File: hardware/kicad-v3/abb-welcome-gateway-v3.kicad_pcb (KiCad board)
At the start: 2 copper layers, 45.3 x 53.3 mm, 69 parts, among them P1 WJ500V-5.08-2P, Q1 S8050, Q2 S8050, Q3 S8050, Q4 2N7002, Q5 2N7002, Q6 2N7002, SW1 TS-1187A-B-A-B, U1 TPS5430DDAR, U2 ESP32-S3-WROOM-1-N16R8, U3 74LVC1G14

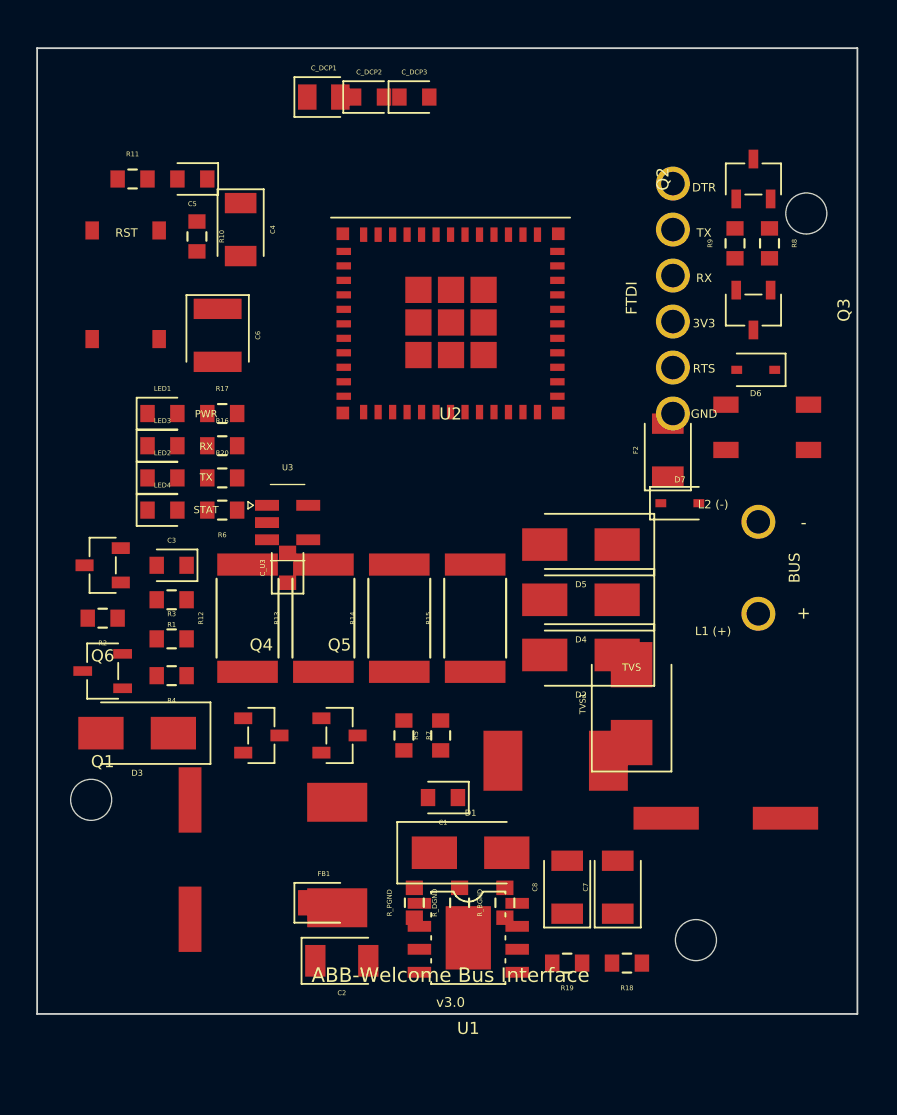
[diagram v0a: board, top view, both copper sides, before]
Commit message: PCB v3: footprint real del ESP32-S3-WROOM-1, placa a 56.4mm y placement listo para rutear
- U2: sustituido el footprint tipo QFN invalido (61 pads inventados) por
  RF_Module:ESP32-S3-WROOM-1 oficial de KiCad; nets remapeados a los pines
  reales del modulo (GND/3V3/EN/IO4/IO5/IO0/RXD0/TXD0/IO2 + EP). Antena al
  borde superior con su keep-out.
- Contorno: +3mm de alto (45.4x56.4) para dar sitio a la banda del buck.
- Placement reorganizado por islas de tierra: DGND arriba (ESP32/FTDI/reset/
  LEDs/U3), BUS_GND banda media y columna derecha (front-end RX/TX, entrada
  28V), PGND abajo (buck TPS5430 con U1 rotado 180: VIN hacia C7/C8, SW
  hacia D1/L2; feedback R18/R19 junto al pin FB; C4/C6 en su isla).
- Star point PGND/DGND/BUS_GND abajo a la derecha (R_PGND/R_BGND/R_DGND).
- Corregidas colisiones fisicas invisibles al DRC (footprints sin courtyard
  ni cuerpo: L2/L3/C19/C23/P1): FB1 bajo L2, TVS1 sobre L3, etc.
- Verificado: 0 solapes de courtyard/envolvente fisica en DRC y chequeo
  propio con cuerpos reales.
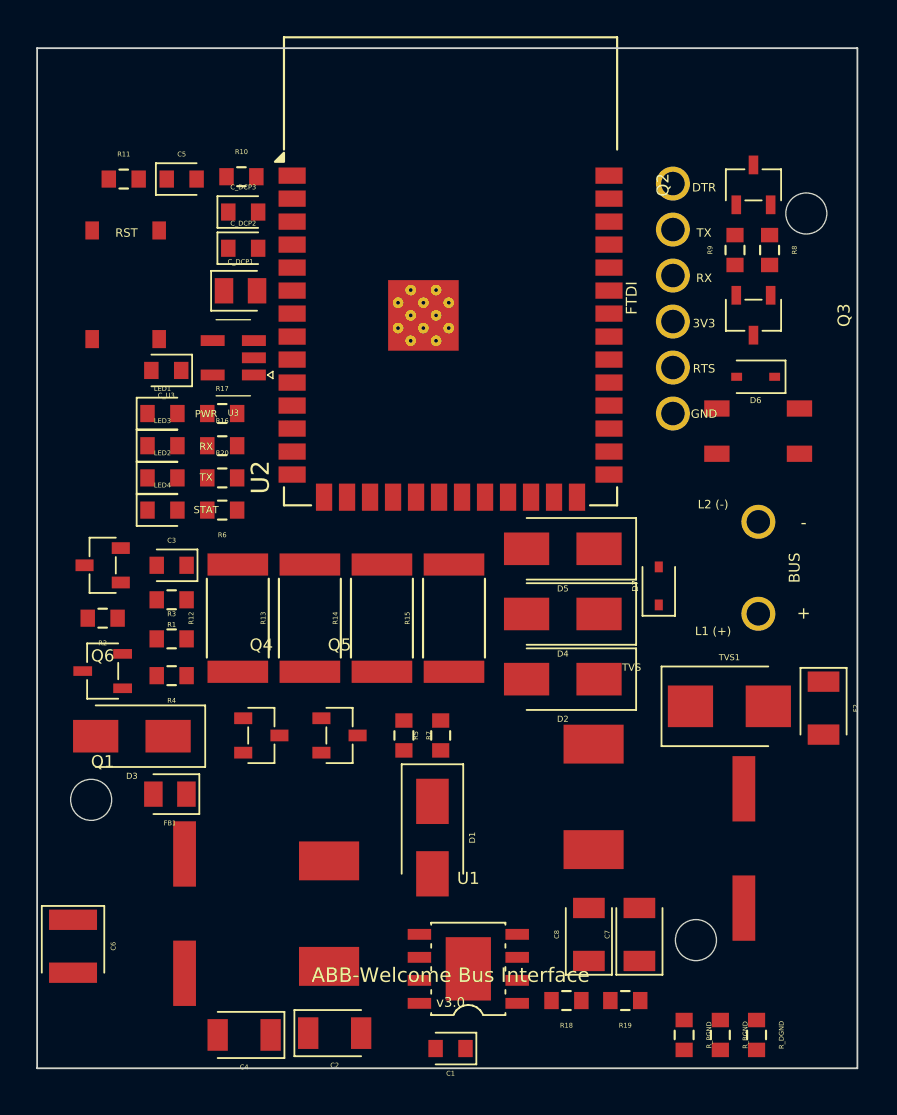
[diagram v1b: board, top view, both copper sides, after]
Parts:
- U2: footprint tscircuit:ESP32-S3-WROOM-1-N16R8 -> ESP32-S3-WROOM-1
- moved C4 44.5 mm to (88.6, 129.3), turned to 180 degrees
- moved C6 34.7 mm to (79.2, 124.4)
- moved R_DGND 18.0 mm to (116.9, 129.3), turned to -90 degrees
- moved F2 16.6 mm to (120.6, 111.2), turned to -90 degrees
- moved R_PGND 16.6 mm to (112.9, 129.3), turned to -90 degrees
- moved R_BGND 14.0 mm to (114.9, 129.3), turned to -90 degrees
- moved C1 13.9 mm to (100.0, 130.1)
- moved C_U3 12.8 mm to (84.3, 92.6), turned to 180 degrees
- moved C_DCP1 11.6 mm to (88.4, 88.2)
- moved C_DCP3 11.4 mm to (88.5, 83.8)
- moved C_DCP2 10.9 mm to (88.5, 85.8)
- moved FB1 10.4 mm to (84.5, 116.0), turned to 180 degrees
- moved U3 9.58 mm to (88.0, 91.9), turned to 180 degrees
- moved TVS1 5.40 mm to (115.4, 111.2), turned to 0 degrees
- moved D7 4.71 mm to (111.5, 104.5), turned to 90 degrees
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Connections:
- U2 pad 27: (no net) -> BOOT_STRAP
- U2 pad 36: (no net) -> RX
- U2 pad 37: (no net) -> TX
- U2 pad 38: BOOT_STRAP -> LED_PIN
- U2 pad 40: (no net) -> DGND
- U2 pad 41: (no net) -> DGND
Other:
- board size 45.3 x 53.3 mm -> 45.3 x 56.3 mm

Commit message: PCB v3: reglas de diseno, net classes y zonas de las 3 islas de GND
- .kicad_pro: minimos 0.2/0.2mm (JLCPCB 2 capas), via 0.6/0.3; clases
  Power (0.8mm), BusHV (0.8mm ancho, 0.5mm clearance para el bus 28V),
  Ground (0.5mm) con asignacion por net.
- Zonas B.Cu: plano DGND (superior + corredor por el borde este hasta el
  star point), banda BUS_GND (front-end + bolsillo de entrada de bus),
  plano PGND (banda inferior del buck). Separacion 0.3mm entre islas.
- Zonas F.Cu: refuerzo PGND (termico del buck) y BUS_GND en el bolsillo.
- El keep-out de antena del modulo mantiene sin cobre la franja superior.
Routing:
- added copper zone on B.Cu, net BUS_GND
- added copper zone on F.Cu, net BUS_GND
- added copper zone on B.Cu, net DGND
- added copper zone on B.Cu, net PGND
- added copper zone on F.Cu, net PGND
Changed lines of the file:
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@@
+		)
+	)
+	(zone
+		(net 40)
+		(net_name "BUS_GND")
+		(layer "F.Cu")
+		(name "BUSGND_top")
+		(hatch edge 0.5)
+		(connect_pads
+			(clearance 0.3)
+		)
+		(min_thickness 0.25)
+		(filled_areas_thickness no)
+		(fill yes
+			(thermal_gap 0.3)
+			(thermal_bridge_width 0.5)
+		)
+		(polygon
+			(pts
+				(xy 104.4 99.15) (xy 119.55 99.15) (xy 119.55 123.3) (xy 104.4 123.3)
+			)
+		)
+	)
+	(zone
+		(net 6)
+		(net_name "PGND")
+		(layer "F.Cu")
+		(name "PGND_top")
+		(hatch edge 0.5)
+		(connect_pads
+			(clearance 0.3)
+		)
+		(min_thickness 0.25)
+		(filled_areas_thickness no)
+		(fill yes
+			(thermal_gap 0.3)
+			(thermal_bridge_width 0.5)
+		)
+		(polygon
+			(pts
+				(xy 77.45 114.9) (xy 104.1 114.9) (xy 104.1 123.75) (xy 119.5 123.75) (xy 119.5 130.85) (xy 77.45 130.85)
+			)
+		)
+	)
+	(zone
+		(net 40)
+		(net_name "BUS_GND")
+		(layer "B.Cu")
+		(name "BUSGND_plane")
+		(hatch edge 0.5)
+		(connect_pads
+			(clearance 0.3)
+		)
+		(min_thickness 0.25)
+		(filled_areas_thickness no)
+		(fill yes
+			(thermal_gap 0.3)
+			(thermal_bridge_width 0.5)
+		)
+		(polygon
+			(pts
+				(xy 77.45 101.75) (xy 100.3 101.75) (xy 100.3 99.15) (xy 119.55 99.15) (xy 119.55 123.3) (xy 104.4 123.3)
+				(xy 104.4 114.45) (xy 77.45 114.45)
+			)
+		)
+	)
+	(zone
+		(net 1)
+		(net_name "DGND")
+		(layer "B.Cu")
+		(name "DGND_plane")
+		(hatch edge 0.5)
+		(connect_pads
+			(clearance 0.3)
+		)
+		(min_thickness 0.25)
+		(filled_areas_thickness no)
+		(fill yes
+			(thermal_gap 0.3)
+			(thermal_bridge_width 0.5)
+		)
+		(polygon
+			(pts
+				(xy 77.45 80.5) (xy 122.15 80.5) (xy 122.15 130.85) (xy 119.85 130.85) (xy 119.85 98.7) (xy 100 98.7)
+				(xy 100 101.3) (xy 77.45 101.3)
+			)
+		)
+	)
+	(zone
+		(net 6)
+		(net_name "PGND")
+		(layer "B.Cu")
+		(name "PGND_plane")
+		(hatch edge 0.5)
+		(connect_pads
+			(clearance 0.3)
+		)
+		(min_thickness 0.25)
+		(filled_areas_thickness no)
+		(fill yes
+			(thermal_gap 0.3)
+			(thermal_bridge_width 0.5)
+		)
+		(polygon
+			(pts
+				(xy 77.45 114.9) (xy 104.1 114.9) (xy 104.1 123.75) (xy 119.5 123.75) (xy 119.5 130.85) (xy 77.45 130.85)
+			)
 		)
 	)

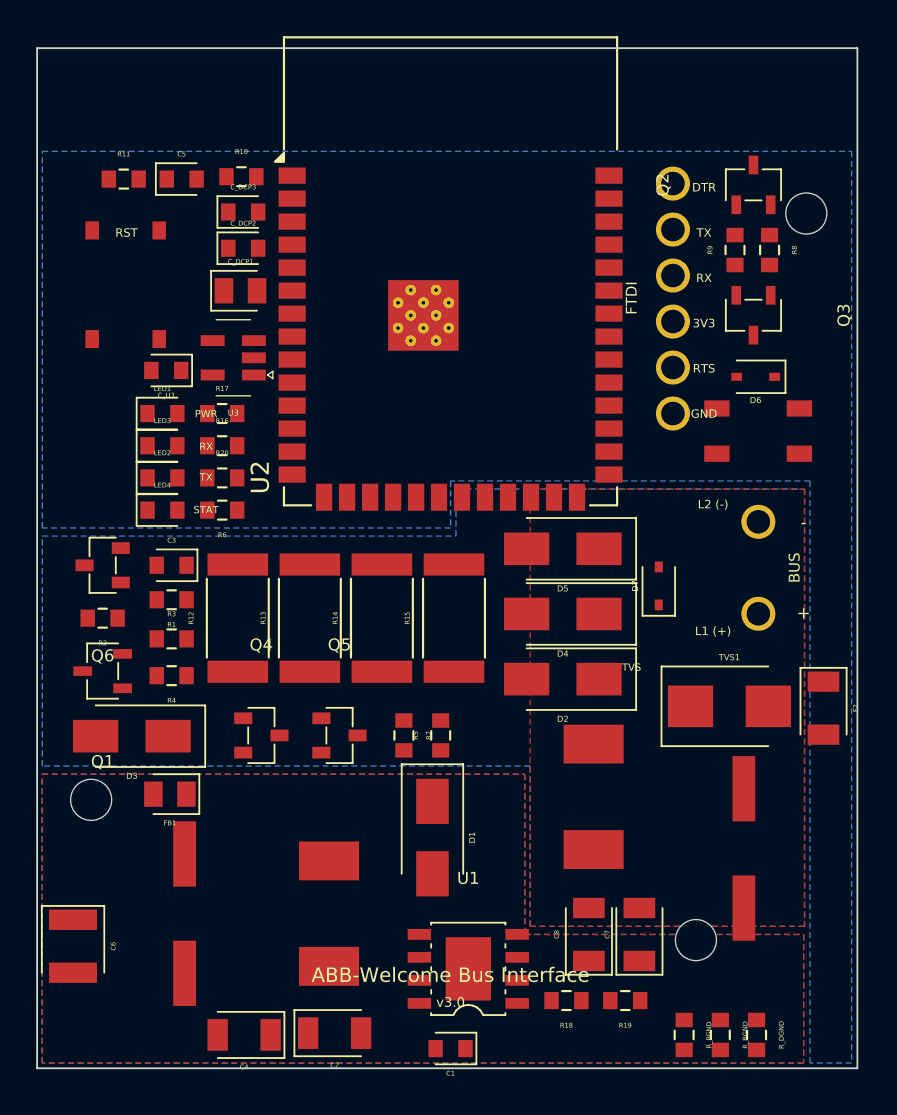
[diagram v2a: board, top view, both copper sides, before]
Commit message: PCB v3: cosido de tierras y ruteo del buck (bloque 1)
- Vias de cosido a plano para todos los pads GND SMD (DGND/BUS_GND/PGND),
  EP del modulo y del TPS5430 con 4 vias cada uno.
- Buck ruteado: VIN (L3->C7/C8->pin2), SW (L2/D1/C1->pin7), bootstrap,
  feedback por B.Cu hasta R18/R19, y distribucion V3V3 (C19/C6/C4/C2/FB1
  y cruce B.Cu hasta R19). Zonas con frontera oeste BUS_GND/PGND ajustada
  y extension norte del bolsillo para la via de L1.3.
- DRC: 0 errores electricos.
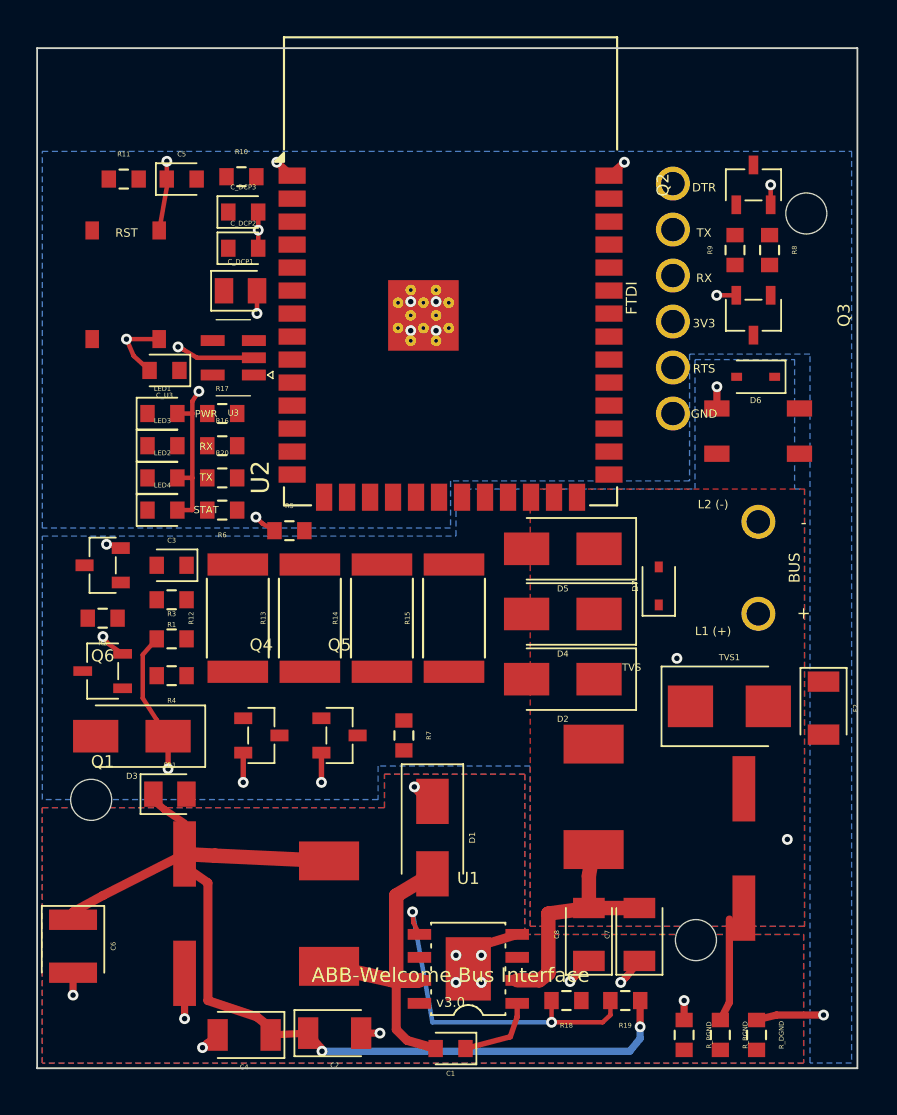
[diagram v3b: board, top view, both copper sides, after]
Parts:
- moved R5 14.1 mm to (91.1, 101.5), turned to 0 degrees
- moved C_U3 0.10 mm to (84.2, 92.6)
- turned FB1 to 0 degrees
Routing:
- net V3V3: track 0.00 -> 53.3 mm, vias 0 -> 2
- net DGND: track 0.00 -> 33.6 mm, vias 0 -> 16
- net BUS_GND: track 0.00 -> 20.3 mm, vias 0 -> 8
- net FB_TAP: track 0.00 -> 18.6 mm, vias 0 -> 2
- net SW_NODE: track 0.00 -> 18.6 mm
- net BUS_PWR: track 0.00 -> 13.5 mm
- net PGND: track 0.00 -> 11.2 mm, vias 0 -> 12
- net BOOT_CAP: track 0.00 -> 4.46 mm

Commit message: PCB v3: ruteo columna ESP32, entrada de bus 28V y front-end RX (bloque 2)
- Columna izquierda del modulo: entradas de pines 2-5 resueltas (V3V3_ESP
  desde R10.2, EN por dorsal B.Cu con via pegada al pad, BUS_RX_PIN en
  zigzag por el hueco de los desacoplos, via-en-pad para GND del modulo).
- Bus 28V: BUS_HOT/BUS_FUSED con salto B.Cu por el corredor este,
  BUS_RTN, cadena BUS_HOT_F en linea recta por la pila D5/D4/D2+D7,
  BUS_DC_RAW a L3 y BUS_PWR TVS1/C23. TVS1 medio paso al oeste.
- Front-end RX completo: BUS_RX_A (carril bajo las 2512), FILT/BIAS/DET
  (DET cruza en diagonal hasta U3), RX_LED_K.
- DRC: 0 errores.
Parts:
- moved TVS1 0.80 mm to (114.6, 111.2)
- moved C_DCP3 0.30 mm to (88.5, 83.5)
- moved R10 0.20 mm to (88.2, 81.9)
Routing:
- net EN: track 0.00 -> 42.3 mm, vias 0 -> 3
- net BUS_FUSED: track 0.00 -> 29.6 mm, vias 0 -> 2
- net BUS_RX_DET: track 0.00 -> 23.1 mm
- net BUS_RX_A: track 0.00 -> 21.1 mm
- net BUS_HOT_F: track 0.00 -> 18.3 mm
- net BUS_PWR: track 13.5 -> 27.1 mm
- net RX_LED_K: track 0.00 -> 11.0 mm
- net BUS_RTN: track 0.00 -> 10.9 mm
- net BUS_RX_PIN: track 0.00 -> 8.90 mm
- net V3V3_ESP: track 0.00 -> 8.48 mm
- net BUS_RX_FILT: track 0.00 -> 6.50 mm
- net BUS_HOT: track 0.00 -> 5.99 mm
- net BUS_DC_RAW: track 0.00 -> 5.82 mm
- net BUS_RX_BIAS: track 0.00 -> 5.30 mm
- net BUS_GND: track 20.3 -> 15.8 mm
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
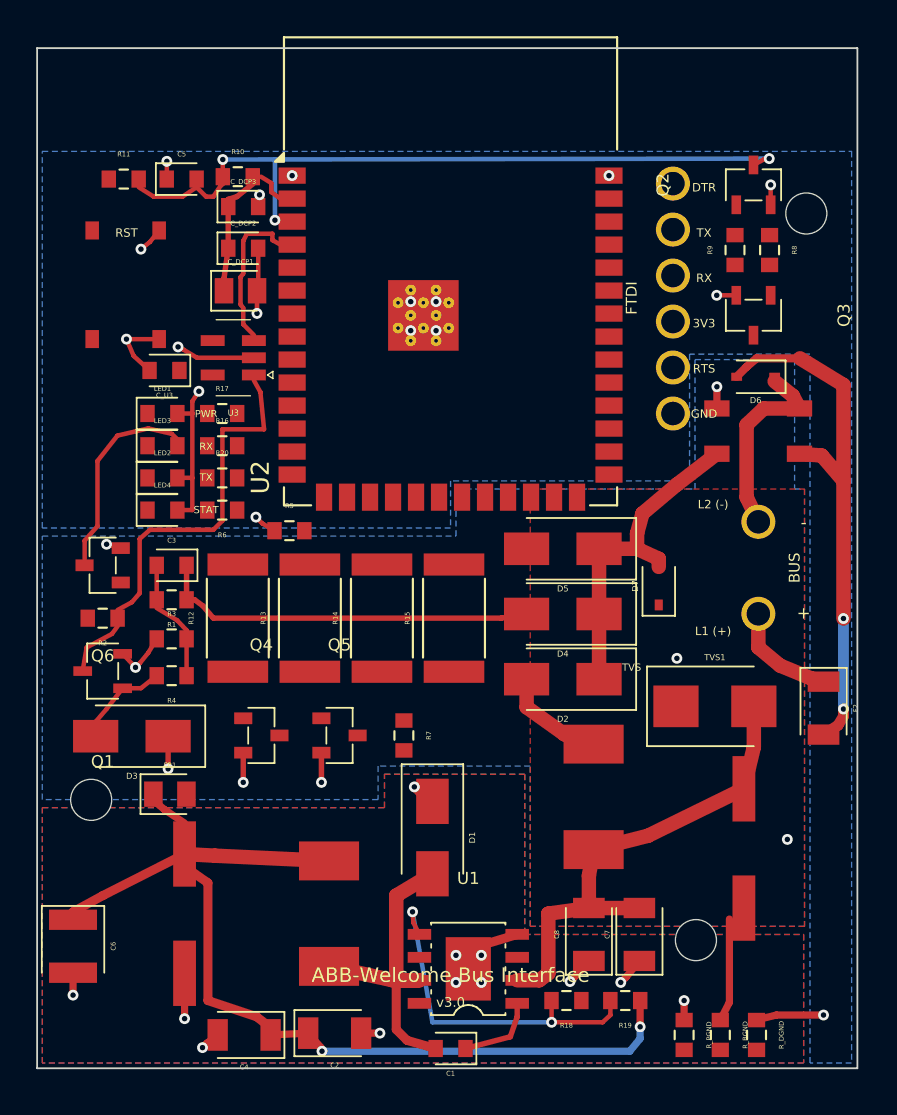
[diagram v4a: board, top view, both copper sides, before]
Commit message: PCB v3: LEDs, reset, tronco V3V3_ESP y cadena TX (bloque 3a)
- LEDs girados 180: catodos al oeste con vias DGND en campo abierto,
  anodos enfrentados a sus resistencias.
- Tronco V3V3_ESP por B.Cu (FB1 -> cluster norte) con ramas a R16/R17
  (via en pad), C_U3/U3.5, R2.2 y enlace del cluster por el hueco de U3.
- BUS_RX_PIN hasta Q6.1 por B.Cu; BUS_TX_PIN completo (canal oeste,
  junction y salto B a R7); TX_GATE rodeando por el sur; drenadores
  y BUS_TX en lineas rectas por los huecos de las 2512.
- DRC: 0 errores.
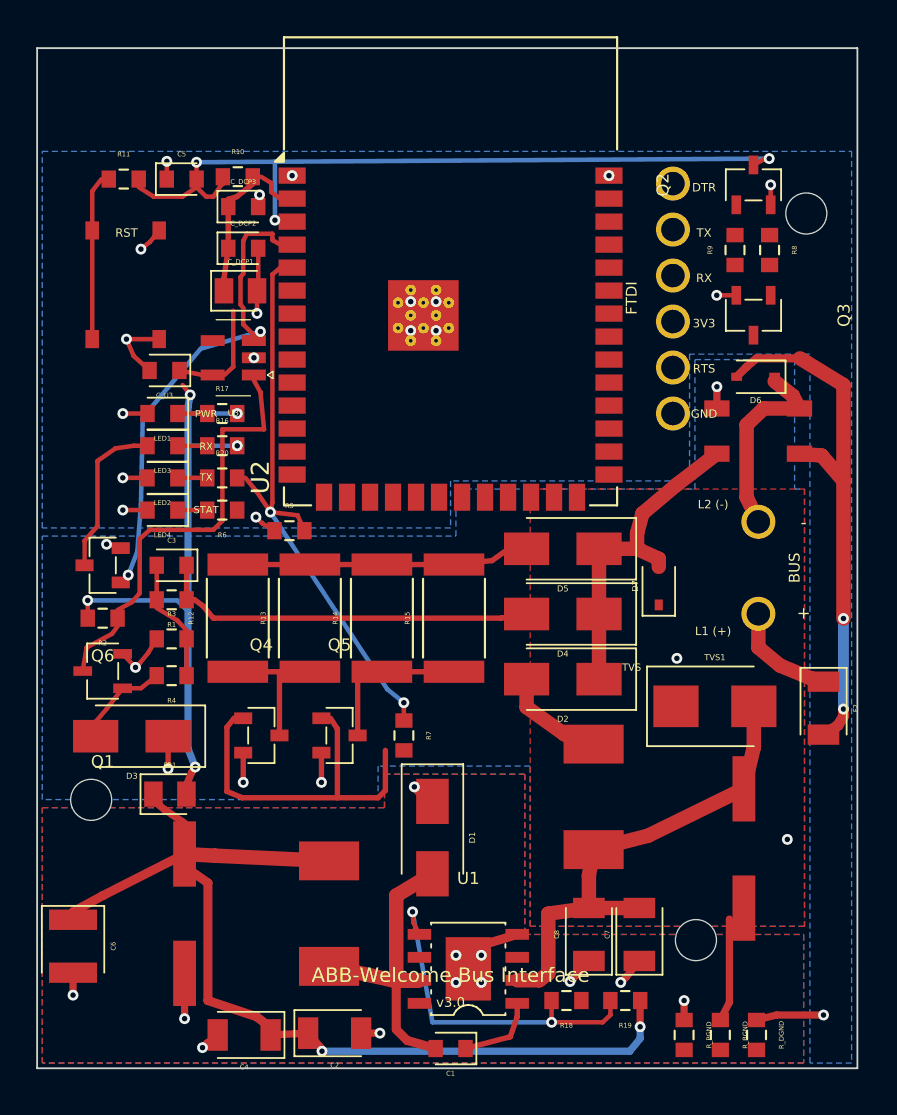
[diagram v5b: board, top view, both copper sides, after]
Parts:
- turned LED1 to 180 degrees
- turned LED2 to 180 degrees
- turned LED3 to 180 degrees
- turned LED4 to 180 degrees
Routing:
- net V3V3_ESP: track 8.48 -> 48.3 mm, vias 0 -> 5
- net BUS_TX_PIN: track 0.00 -> 33.0 mm, vias 0 -> 2
- net TX_GATE: track 0.00 -> 20.4 mm
- net BUS_RX_PIN: track 8.90 -> 27.1 mm, vias 0 -> 2
- net BUS_TX: track 0.00 -> 16.2 mm
- net DGND: track 31.4 -> 22.0 mm, vias 17 -> 19
- net RST_BTN: track 0.00 -> 9.01 mm
- net TX_DRAIN_B: track 0.00 -> 8.84 mm
- net TX_DRAIN_A: track 0.00 -> 7.50 mm
- net RX_LED_K: track 11.0 -> 8.67 mm
- net TX_LED_A: track 0.00 -> 1.65 mm
- net STAT_LED_A: track 0.00 -> 1.65 mm
- net RX_LED_A: track 0.00 -> 1.65 mm
- net PWR_LED_A: track 0.00 -> 1.65 mm
- net EN: track 42.3 -> 43.2 mm

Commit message: PCB v3: ruteo completo — DRC limpio y ratsnest a cero
- Lado derecho: BOOT_STRAP, RTS (R8 movido junto al taladro, via en pad),
  DTR, EN_DRIVE, D0_DRIVE, UART RX/TX, BUS_HOT_F v2 y puente GND del star.
- LED_PIN reasignado del pin 38 (IO2) al pin 6 (IO6) del modulo: el
  cuadrante de P2 es intransitable (anillos THT cada 2.54mm); con IO6 la
  ruta queda en B.Cu directa a R6. EL FIRMWARE DEBE USAR GPIO6.
- V3V3_ESP a P2.3 desde via-en-pad del pin 2 por carril B bajo el modulo.
- Puentes DGND para reunificar el plano B (franja bajo modulo y zona este
  selladas por la dorsal EN y los anillos de P2).
- kicad-cli drc: 0 errores, 0 unconnected.
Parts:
- moved R8 4.04 mm to (119.3, 89.6), turned to 90 degrees
- turned R9 to -90 degrees
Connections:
- U2 pad 38: LED_PIN -> (no net)
- U2 pad 6: (no net) -> LED_PIN
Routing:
- net V3V3_ESP: track 48.3 -> 74.9 mm, vias 5 -> 6
- net DGND: track 22.0 -> 39.4 mm, vias 19 -> 23
- net LED_PIN: track 0.00 -> 14.6 mm, vias 0 -> 2
- net BOOT_STRAP: track 0.00 -> 12.1 mm, vias 0 -> 2
- net RTS: track 0.00 -> 8.27 mm, vias 0 -> 1
- net EN_DRIVE: track 0.00 -> 6.18 mm
- net DTR: track 0.00 -> 5.07 mm
- net GND: track 0.00 -> 4.00 mm
- net TX: track 0.00 -> 3.85 mm
- net RX: track 0.00 -> 3.64 mm
- net D0_DRIVE: track 0.00 -> 2.91 mm
- net TX_GATE: track 20.4 -> 21.4 mm
- net BUS_HOT_F: track 18.3 -> 19.1 mm
- net BUS_GND: track 15.8 -> 15.0 mm
